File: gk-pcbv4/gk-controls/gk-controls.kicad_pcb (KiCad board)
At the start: 2 copper layers, 120.6 x 72.2 mm, 110 parts, among them J1 Conn_01x20, J10 Conn_01x01, J2 Conn_01x03, J3 Conn_01x01, J4 Conn_01x01, J5 Conn_01x01, J6 Conn_01x01, J7 Conn_01x06, J8 Conn_01x01, J9 Conn_01x01, U1 PCAL6416APW, U2 ULN2003A, U3 LMV358DMR2G, U4 LMV358DMR2G

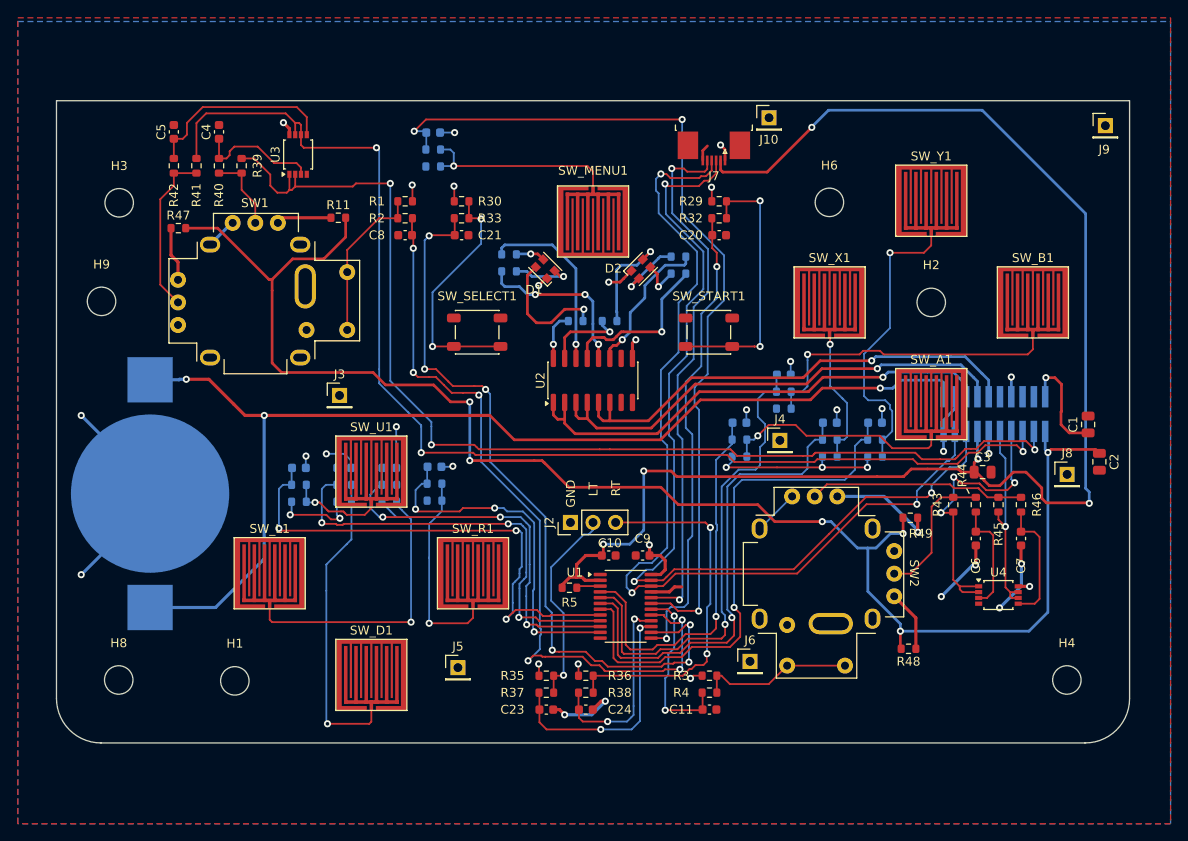
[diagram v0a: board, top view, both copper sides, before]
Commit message: update controls layout triggers now are analog new ADC on control board Move bumper buttons to trigger daughterboard and put in more ergonomical position
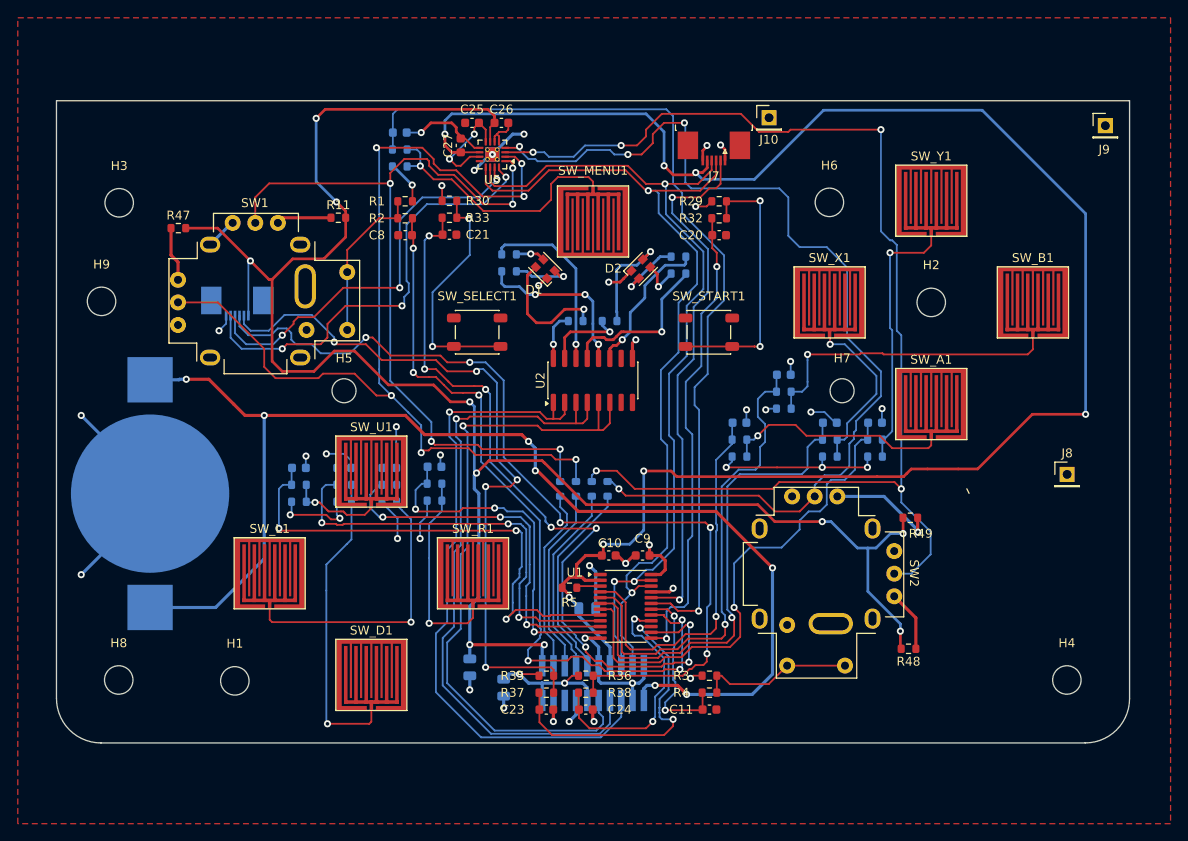
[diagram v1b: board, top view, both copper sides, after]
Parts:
- removed C4, C5, C6, C7: 100n, Capacitor_SMD:C_0603_1608Metric
- removed J2: Conn_01x03, Connector_PinHeader_2.54mm:PinHeader_1x03_P2.54mm_Vertical
- removed J3, J4, J5, J6: Conn_01x01, Connector_PinHeader_2.54mm:PinHeader_1x01_P2.54mm_Vertical
- removed R39, R41, R43, R45: NC, Resistor_SMD:R_0603_1608Metric
- removed R40, R42, R44, R46: 20k, Resistor_SMD:R_0603_1608Metric
- removed U3, U4: LMV358DMR2G, Package_SO:OnSemi_Micro8
- added C25: 1u, Capacitor_SMD:C_0603_1608Metric, F.Cu at (136.4, 62.5)
- added C26: 1u, Capacitor_SMD:C_0603_1608Metric, F.Cu at (139.7, 62.5)
- added C27: 1u, Capacitor_SMD:C_0603_1608Metric, F.Cu at (135.1, 65.0)
- added H5: MountingHole, MountingHole:MountingHole_2.7mm_M2.5, F.Cu at (122.0, 92.6)
- added H7: MountingHole, MountingHole:MountingHole_2.7mm_M2.5, F.Cu at (178.0, 92.6)
- added J11: Conn_01x06, Connector_FFC-FPC:TE_0-1734839-6_1x06-1MP_P0.5mm_Horizontal, B.Cu at (110.0, 82.8)
- added R50: NC, Resistor_SMD:R_0603_1608Metric, B.Cu at (148.1, 103.6)
- added R51: NC, Resistor_SMD:R_0603_1608Metric, B.Cu at (146.3, 103.6)
- added R52: NC, Resistor_SMD:R_0603_1608Metric, B.Cu at (149.9, 103.6)
- added R53: NC, Resistor_SMD:R_0603_1608Metric, B.Cu at (151.6, 103.6)
- added U5: ~, Package_DFN_QFN:WQFN-16-1EP_3x3mm_P0.5mm_EP1.6x1.6mm_ThermalVias, F.Cu at (138.7, 66.0)
- C1, C2, C3: moved to B.Cu
- R11, R47, R48, R49: value 10k -> 10k/0R
- moved C2 74.5 mm to (136.1, 123.7)
- moved C1 72.1 mm to (140.0, 126.0), turned to -90 degrees
- moved J1 54.3 mm to (150.0, 125.5), turned to -90 degrees
- moved C3 47.0 mm to (149.4, 117.1)
- moved C22 3.76 mm to (128.3, 63.6)
- moved R31 3.76 mm to (128.3, 67.4)
- moved R34 3.76 mm to (128.3, 65.5)
- moved C21 1.37 mm to (133.9, 75.1)
- moved R30 1.37 mm to (133.9, 71.2)
- moved R33 1.37 mm to (133.9, 73.2)
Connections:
- net BTN_MCU_LT renamed BTN_MCU_LB
- net BTN_MCU_RT renamed BTN_MCU_RB
- net Net-(J2-Pin_2) renamed BTN_LB
- net Net-(J2-Pin_3) renamed BTN_RB
- J1 pad 3: JOY_A_X_MCU -> Net-(J1-Pin_3)
- J1 pad 5: JOY_A_Y_MCU -> Net-(J1-Pin_5)
- J1 pad 7: JOY_B_X_MCU -> Net-(J1-Pin_7)
- J1 pad 9: JOY_B_Y_MCU -> Net-(J1-Pin_9)
- J7 pad 1: +3V3 -> GND
- J7 pad 2: VDDIO -> Net-(J7-Pin_2)
- J7 pad 3: I2C1_SDA -> I2C1_SCL
- J7 pad 4: I2C1_SCL -> I2C1_SDA
- J7 pad 5: Net-(J7-Pin_5) -> VDDIO
- J7 pad 6: GND -> +3V3
- U1 pad 20: Net-(J7-Pin_5) -> Net-(J7-Pin_2)
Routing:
- net JOY_A_Y_MCU: track 137.2 -> 0.00 mm, vias 3 -> 0
- net JOY_A_X_MCU: track 126.1 -> 0.00 mm, vias 3 -> 0
- net JOY_B_X: track 15.8 -> 138.2 mm, vias 0 -> 5
- net JOY_A_Y: track 18.5 -> 112.1 mm, vias 0 -> 6
- net JOY_B_Y: track 24.4 -> 112.2 mm, vias 0 -> 4
- net JOY_A_X: track 8.77 -> 91.6 mm, vias 0 -> 5
- net BTN_RB: track 41.5 -> 102.3 mm, vias 2 -> 5
- net Net-(J7-Pin_2): track 0.00 -> 60.7 mm, vias 0 -> 2
- net Net-(J7-Pin_5): track 60.5 -> 0.00 mm, vias 2 -> 0
- net BTN_LB: track 23.1 -> 80.5 mm, vias 1 -> 5
- net RT_ANA: track 0.00 -> 49.8 mm, vias 0 -> 3
- net LT_ANA: track 0.00 -> 45.7 mm, vias 0 -> 3
- net VDDIO: track 164.7 -> 204.6 mm, vias 5 -> 7
- net VDDA: track 176.7 -> 211.1 mm, vias 6 -> 10
- net JOY_B_X_MCU: track 33.1 -> 0.00 mm, vias 3 -> 0
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- added copper zone on In2.Cu, net +3V3
- added copper zone on In1.Cu, net GND
- removed copper zone on B.Cu, net +3V3
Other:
- copper layers 2 -> 4
- board text removed: "GND"
- board text removed: "LT"
- board text removed: "RT"
